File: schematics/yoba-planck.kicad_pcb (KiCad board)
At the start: 2 copper layers, 60 parts, among them M1 AUDIO-JACK3, M2 AUDIO-JACK3, M3 ARDUINO_PRO_MICRO, SW1 SW_PUSH, SW10 SW_PUSH, SW11 SW_PUSH, SW12 SW_PUSH, SW13 SW_PUSH, SW14 SW_PUSH, SW15 SW_PUSH, SW16 SW_PUSH, SW17 SW_PUSH, SW18 SW_PUSH, SW19 SW_PUSH, SW2 SW_PUSH, SW20 SW_PUSH, SW21 SW_PUSH, SW22 SW_PUSH, SW23 SW_PUSH, SW24 SW_PUSH, SW3 SW_PUSH, SW4 SW_PUSH, SW5 SW_PUSH, SW6 SW_PUSH, SW7 SW_PUSH, SW8 SW_PUSH, SW9 SW_PUSH

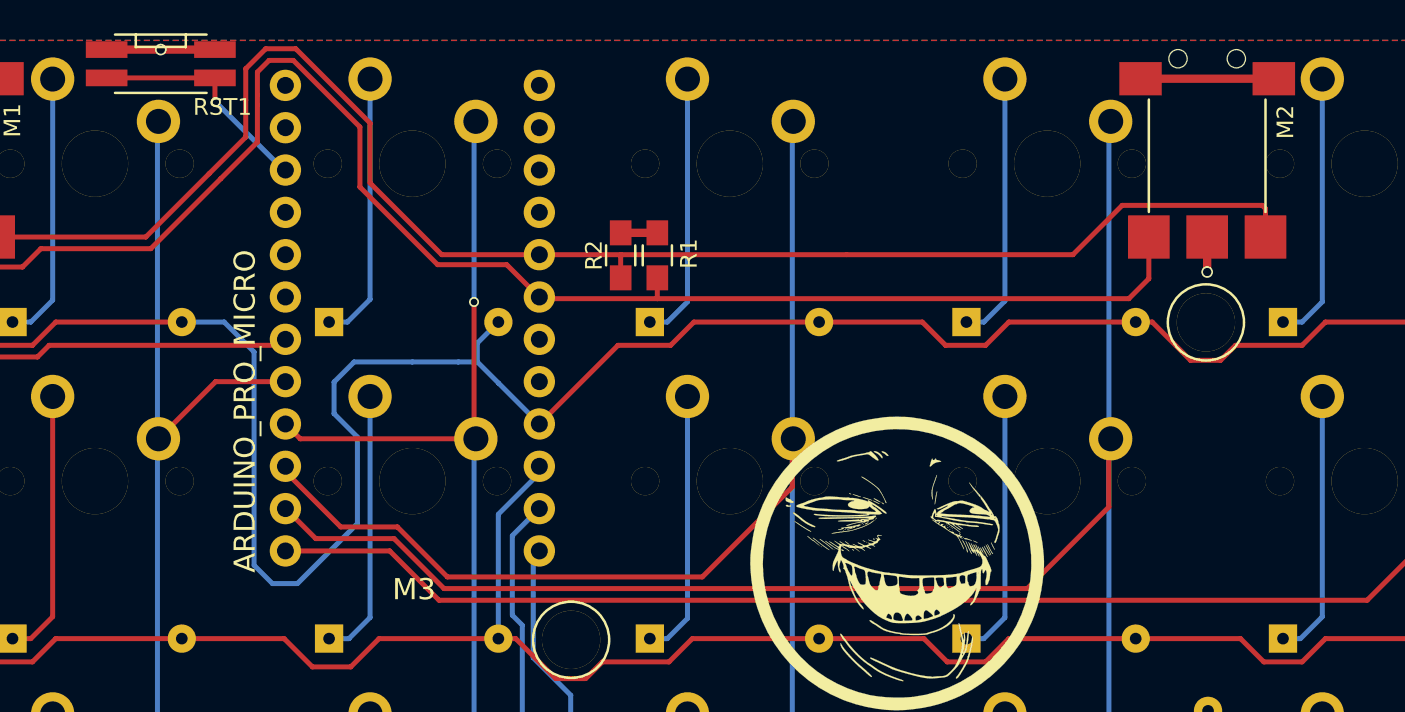
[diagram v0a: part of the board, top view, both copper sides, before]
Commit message: series resistance added to i2c bus
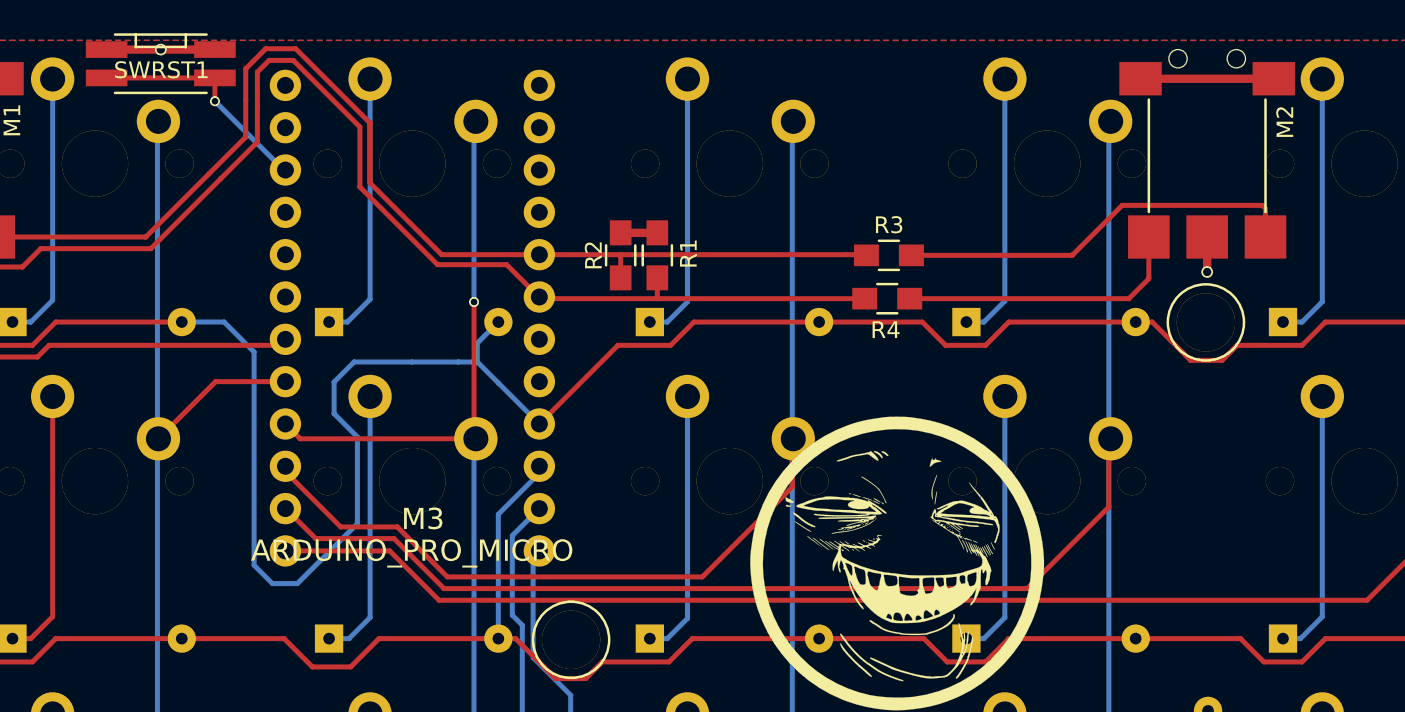
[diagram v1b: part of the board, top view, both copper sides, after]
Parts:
- removed RST1: SW_PUSH, yoba:edgeswbut
- added R3: 22, Resistors_SMD:R_0805_HandSoldering, F.Cu at (180.7, 75.5)
- added R4: 22, Resistors_SMD:R_0805_HandSoldering, F.Cu at (180.6, 78.1)
- added SWRST1: SW_PUSH, yoba:edgeswbut, F.Cu at (137.0, 64.0)
- M3: footprint SparkFun-Boards:ARDUINO_PRO_MICRO -> yoba:ARDUINO_PRO_MICRO
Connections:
- M2 pad 2: sda -> Net-(M2-Pad2)
- M2 pad 3: scl -> Net-(M2-Pad3)
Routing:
- net sda: track 95.1 -> 68.1 mm
- net Net-(M2-Pad2): track 0.00 -> 24.3 mm
- net scl: track 97.9 -> 77.6 mm
- net Net-(M2-Pad3): track 0.00 -> 17.5 mm

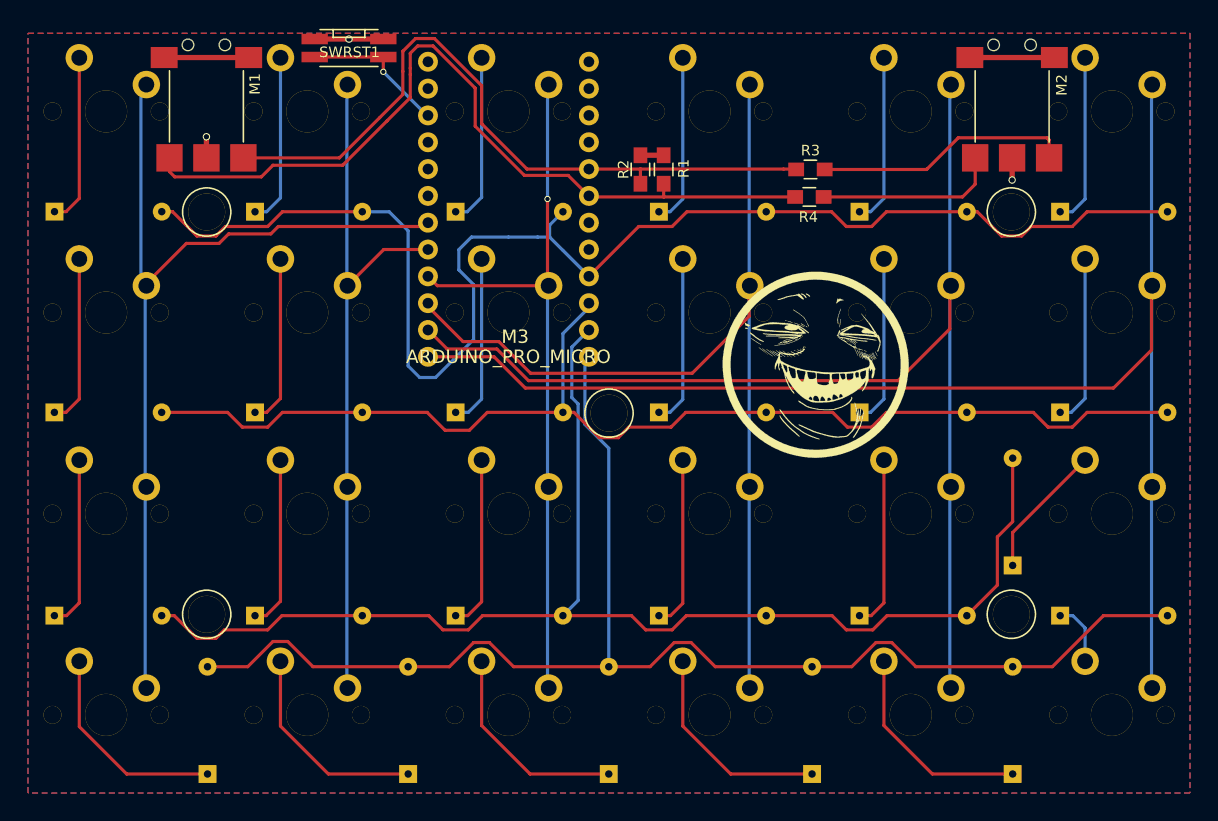
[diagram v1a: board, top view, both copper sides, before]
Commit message: Logo updated, layout improoved, mouting holes enlarged
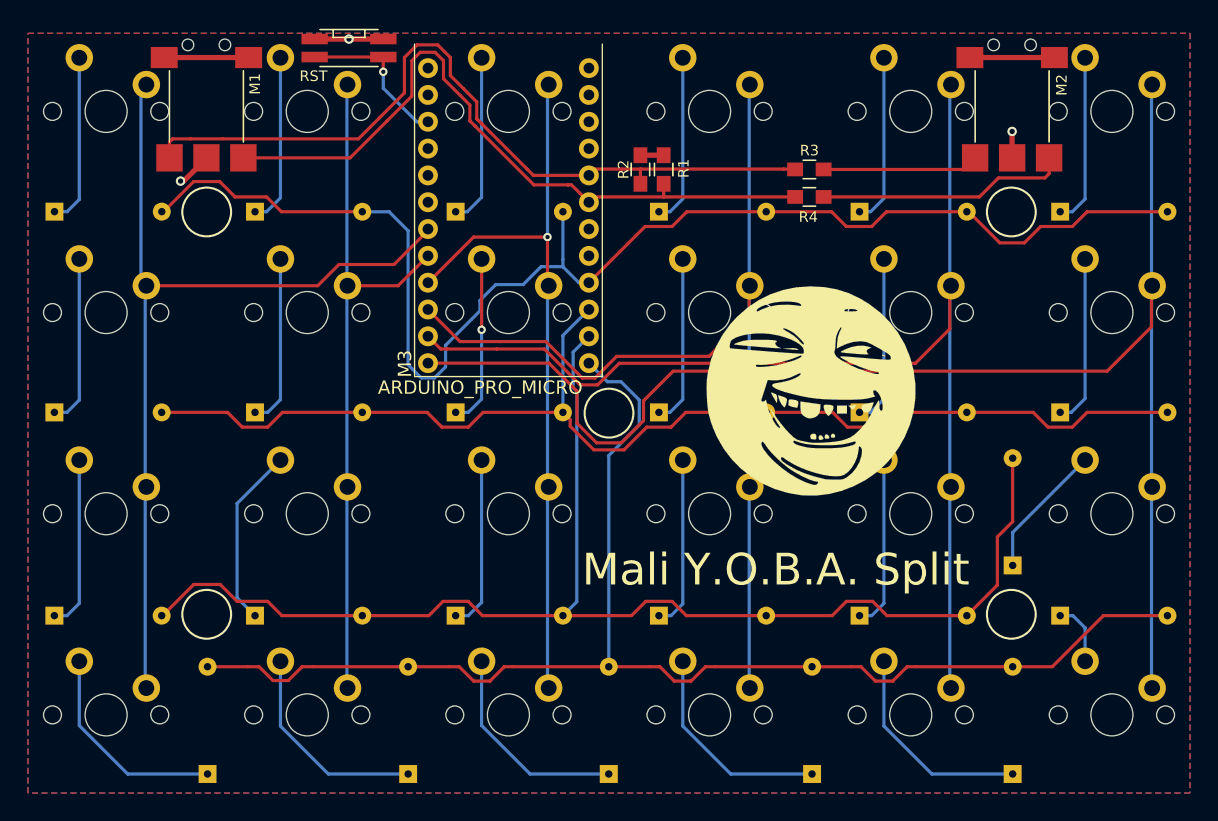
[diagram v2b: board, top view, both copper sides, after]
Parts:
- moved G*** 2.52 mm to (180.8, 96.5), turned to 0 degrees
- moved M3 0.60 mm to (152.1, 78.6)
- moved R3 0.10 mm to (180.6, 75.5)
- renumbered SWRST1 to RST
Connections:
- M1 pad 2: sda -> scl
- M1 pad 3: scl -> sda
- M3 pad 3: (no net) -> GND
- M3 pad 4: (no net) -> GND
- R3 pad 1: Net-(M2-Pad2) -> Net-(M2-Pad3)
- R4 pad 1: Net-(M2-Pad3) -> Net-(M2-Pad2)
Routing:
- net scl: track 77.6 -> 67.6 mm
- net sda: track 68.1 -> 75.3 mm
- net col5: track 134.7 -> 140.2 mm
- net row0: track 133.7 -> 130.5 mm
- net Net-(M2-Pad3): track 17.5 -> 14.9 mm
- net GND: track 10.6 -> 12.4 mm
- net col2: track 68.9 -> 70.2 mm
- net Net-(M3-Pad22): track 13.8 -> 15.0 mm
- net row3: track 131.0 -> 130.0 mm
- net Net-(D7-Pad1): track 16.3 -> 17.1 mm
- net Net-(M2-Pad2): track 24.3 -> 23.8 mm
- net Net-(D10-Pad1): vias 0 -> 1
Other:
- net class Default: via_dia 0.6 -> 0.8
- net class power: via_dia 0.7 -> 0.9
- board text added: "Mali Y.O.B.A. Split"

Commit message: fixed board outline
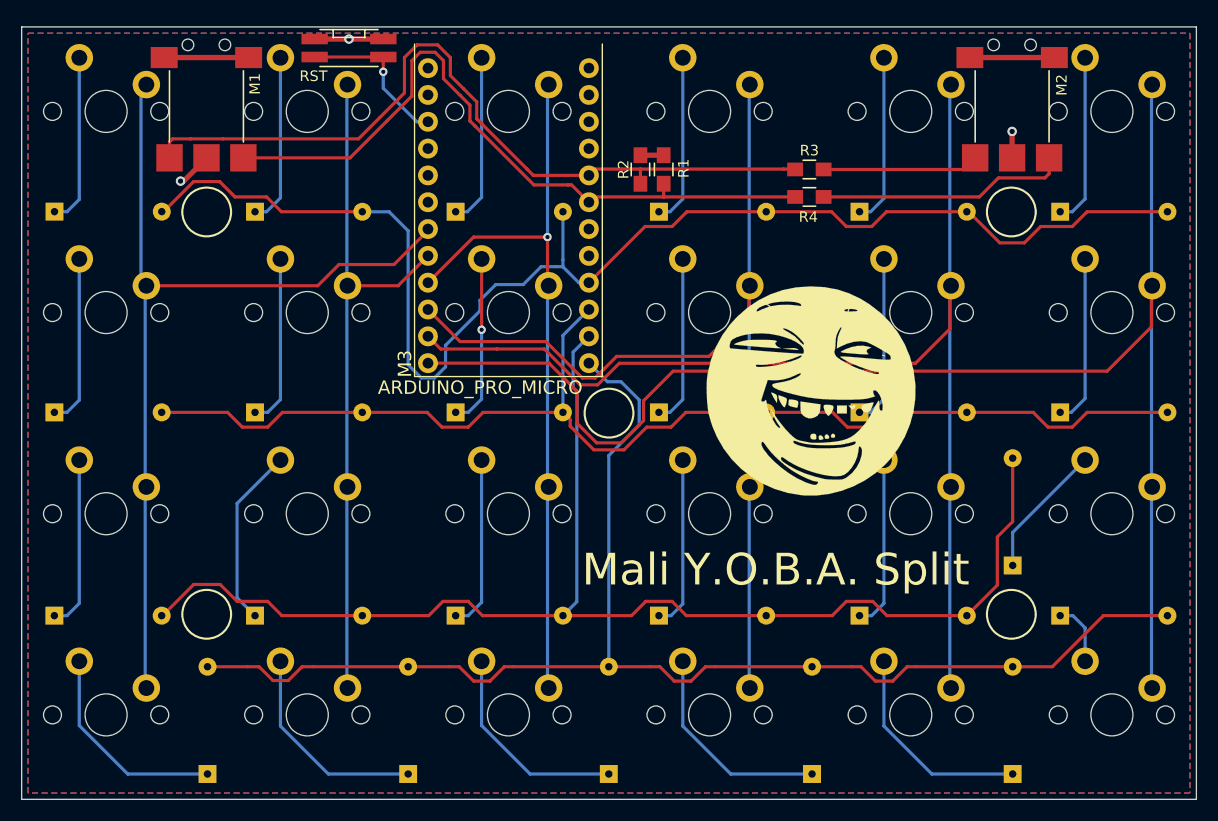
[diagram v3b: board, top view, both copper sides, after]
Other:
- board outline added: 111.2 x 73.2 mm
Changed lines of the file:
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@@
     (links 94)
     (no_connects 0)
-    (area 105.889499 56.15 229.35 138.0291)
+    (area 105.889499 56.45 227.15 138.0291)
     (thickness 1.6)
-    (drawings 9)
+    (drawings 7)
     (tracks 387)
     (zones 0)
@@
       (xy -4.275171 -4.863703)) (layer F.SilkS) (width 0.01))
   )
-  (gr_line (start 217 62) (end 217.25 62) (angle 90) (layer F.Fab) (width 0.2))
-  (gr_line (start 217.25 135.15) (end 217.25 135) (angle 90) (layer F.Fab) (width 0.2))
-  (gr_line (start 217 135.15) (end 217.25 135.15) (angle 90) (layer F.Fab) (width 0.2))
-  (gr_line (start 106 135) (end 106 135.15) (angle 90) (layer F.Fab) (width 0.2))
+  (dimension 111.25 (width 0.3) (layer F.Fab)
+    (gr_text "111.250 mm" (at 161.625 57.8) (layer F.Fab)
+      (effects (font (size 1.5 1.5) (thickness 0.3)))
+    )
+    (feature1 (pts (xy 106 62) (xy 106 56.45)))
+    (feature2 (pts (xy 217.25 62) (xy 217.25 56.45)))
+    (crossbar (pts (xy 217.25 59.15) (xy 106 59.15)))
+    (arrow1a (pts (xy 106 59.15) (xy 107.126504 58.563579)))
+    (arrow1b (pts (xy 106 59.15) (xy 107.126504 59.736421)))
+    (arrow2a (pts (xy 217.25 59.15) (xy 216.123496 58.563579)))
+    (arrow2b (pts (xy 217.25 59.15) (xy 216.123496 59.736421)))
+  )
+  (dimension 73.15 (width 0.3) (layer F.Fab)
+    (gr_text "73.150 mm" (at 220.65 98.575 270) (layer F.Fab)
+      (effects (font (size 1.5 1.5) (thickness 0.3)))
+    )
+    (feature1 (pts (xy 217.25 135.15) (xy 222 135.15)))
+    (feature2 (pts (xy 217.25 62) (xy 222 62)))
+    (crossbar (pts (xy 219.3 62) (xy 219.3 135.15)))
+    (arrow1a (pts (xy 219.3 135.15) (xy 218.713579 134.023496)))
+    (arrow1b (pts (xy 219.3 135.15) (xy 219.886421 134.023496)))
+    (arrow2a (pts (xy 219.3 62) (xy 218.713579 63.126504)))
+    (arrow2b (pts (xy 219.3 62) (xy 219.886421 63.126504)))
+  )
+  (gr_line (start 217.25 62) (end 106 62) (angle 90) (layer Edge.Cuts) (width 0.1))
+  (gr_line (start 217.25 135.15) (end 106 135.15) (angle 90) (layer Edge.Cuts) (width 0.1))
+  (gr_line (start 217.25 62) (end 217.25 135.15) (angle 90) (layer Edge.Cuts) (width 0.1))
+  (gr_line (start 106 135.15) (end 106 62) (angle 90) (layer Edge.Cuts) (width 0.1))
   (gr_text "Mali Y.O.B.A. Split" (at 177.419 113.411) (layer F.SilkS)
     (effects (font (size 3 3) (thickness 0.4)))
   )
-  (gr_line (start 217.25 62) (end 217.25 135) (angle 90) (layer F.Fab) (width 0.2))
-  (gr_line (start 106 62) (end 217 62) (angle 90) (layer F.Fab) (width 0.2))
-  (gr_line (start 106 135) (end 106 62) (angle 90) (layer F.Fab) (width 0.2))
-  (gr_line (start 106 135.15) (end 217 135.15) (angle 90) (layer F.Fab) (width 0.2))
   (segment (start 123.5 74.4) (end 123.5 74.448048) (width 0.5) (layer F.Cu) (net 1))
   (segment (start 123.5 74.448048) (end 121.348048 76.6) (width 0.5) (layer F.Cu) (net 1))

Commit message: rev2
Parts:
- added C1: C, Capacitors_SMD:C_0805_HandSoldering, F.Cu at (179.7, 67.5)
- added D25: LED, mx1a:MX1A-led, F.Cu at (114.0, 70.0)
- added D26: LED, mx1a:MX1A-led, F.Cu at (114.0, 89.0)
- added D27: LED, mx1a:MX1A-led, F.Cu at (114.0, 108.1)
- added D28: LED, mx1a:MX1A-led, F.Cu at (114.0, 127.2)
- added D29: LED, mx1a:MX1A-led, F.Cu at (133.1, 70.0)
- added D30: LED, mx1a:MX1A-led, F.Cu at (133.1, 89.0)
- added D31: LED, mx1a:MX1A-led, F.Cu at (133.1, 108.1)
- added D32: LED, mx1a:MX1A-led, F.Cu at (133.1, 127.2)
- added D33: LED, mx1a:MX1A-led, F.Cu at (152.1, 70.0)
- added D34: LED, mx1a:MX1A-led, F.Cu at (152.1, 89.0)
- added D35: LED, mx1a:MX1A-led, F.Cu at (152.1, 108.1)
- added D36: LED, mx1a:MX1A-led, F.Cu at (152.1, 127.2)
- added D37: LED, mx1a:MX1A-led, F.Cu at (171.2, 70.0)
- added D38: LED, mx1a:MX1A-led, F.Cu at (171.2, 89.0)
- added D39: LED, mx1a:MX1A-led, F.Cu at (171.2, 108.1)
- added D40: LED, mx1a:MX1A-led, F.Cu at (171.2, 127.2)
- added D41: LED, mx1a:MX1A-led, F.Cu at (190.2, 70.0)
- added D42: LED, mx1a:MX1A-led, F.Cu at (190.2, 89.0)
- added D43: LED, mx1a:MX1A-led, F.Cu at (190.2, 108.1)
- added D44: LED, mx1a:MX1A-led, F.Cu at (190.2, 127.2)
- added D45: LED, mx1a:MX1A-led, F.Cu at (209.2, 70.0)
- added D46: LED, mx1a:MX1A-led, F.Cu at (209.2, 89.0)
- added D47: LED, mx1a:MX1A-led, F.Cu at (209.2, 108.1)
- added D48: LED, mx1a:MX1A-led, F.Cu at (209.2, 127.2)
- added Q1: BS170, TO_SOT_Packages_SMD:SOT-23_Handsoldering, F.Cu at (140.8, 83.4)
- added R10: 1k, Resistors_SMD:R_0805_HandSoldering, F.Cu at (131.7, 97.7)
- added R11: 1k, Resistors_SMD:R_0805_HandSoldering, F.Cu at (131.7, 116.7)
- added R12: 1k, Resistors_SMD:R_0805_HandSoldering, F.Cu at (129.7, 130.9)
- added R13: 1k, Resistors_SMD:R_0805_HandSoldering, F.Cu at (153.3, 79.0)
- added R14: 1k, Resistors_SMD:R_0805_HandSoldering, F.Cu at (150.7, 97.8)
- added R15: 1k, Resistors_SMD:R_0805_HandSoldering, F.Cu at (150.7, 116.7)
- added R16: 1k, Resistors_SMD:R_0805_HandSoldering, F.Cu at (148.7, 130.9)
- added R17: 1k, Resistors_SMD:R_0805_HandSoldering, F.Cu at (169.8, 78.6)
- added R18: 1k, Resistors_SMD:R_0805_HandSoldering, F.Cu at (169.8, 97.7)
- added R19: 1k, Resistors_SMD:R_0805_HandSoldering, F.Cu at (169.8, 116.7)
- added R20: 1k, Resistors_SMD:R_0805_HandSoldering, F.Cu at (167.7, 130.9)
- added R21: 1k, Resistors_SMD:R_0805_HandSoldering, F.Cu at (188.9, 78.6)
- added R22: 1k, Resistors_SMD:R_0805_HandSoldering, F.Cu at (188.9, 97.7)
- added R23: 1k, Resistors_SMD:R_0805_HandSoldering, F.Cu at (188.9, 116.7)
- added R24: 1k, Resistors_SMD:R_0805_HandSoldering, F.Cu at (186.8, 130.9)
- added R25: 1k, Resistors_SMD:R_0805_HandSoldering, F.Cu at (207.9, 78.6)
- added R26: 1k, Resistors_SMD:R_0805_HandSoldering, F.Cu at (207.9, 97.6)
- added R27: 1k, Resistors_SMD:R_0805_HandSoldering, F.Cu at (207.9, 116.8)
- added R28: 1k, Resistors_SMD:R_0805_HandSoldering, F.Cu at (205.8, 130.9)
- added R5: 1k, Resistors_SMD:R_0805_HandSoldering, F.Cu at (112.7, 78.7)
- added R6: 1k, Resistors_SMD:R_0805_HandSoldering, F.Cu at (112.7, 97.7)
- added R7: 1k, Resistors_SMD:R_0805_HandSoldering, F.Cu at (112.7, 116.7)
- added R8: 1k, Resistors_SMD:R_0805_HandSoldering, F.Cu at (110.6, 130.9)
- added R9: 1k, Resistors_SMD:R_0805_HandSoldering, F.Cu at (131.7, 78.7)
- M3: moved to F.Cu
- moved RST1 38.4 mm to (175.4, 64.0)
- moved R3 32.4 mm to (148.2, 74.4), turned to 270 degrees
- moved R4 29.8 mm to (150.8, 79.0), turned to 270 degrees
- moved D10 10.2 mm to (157.2, 98.5), turned to 180 degrees
- moved D11 10.2 mm to (157.2, 117.8), turned to 180 degrees
- moved D13 10.2 mm to (176.5, 79.5), turned to 180 degrees
- moved D14 10.2 mm to (176.5, 98.5), turned to 180 degrees
- moved D15 10.2 mm to (176.5, 117.8), turned to 180 degrees
- moved D17 10.2 mm to (195.5, 79.5), turned to 180 degrees
- moved D18 10.2 mm to (195.5, 98.5), turned to 180 degrees
- moved D19 10.2 mm to (195.5, 117.8), turned to 180 degrees
- moved D2 10.2 mm to (119.2, 98.5), turned to 180 degrees
- moved D21 10.2 mm to (214.5, 79.5), turned to 180 degrees
- moved D22 10.2 mm to (214.5, 98.5), turned to 180 degrees
- moved D3 10.2 mm to (119.2, 117.8), turned to 180 degrees
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- renumbered RST to RST1
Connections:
- D1 pad 1: Net-(D1-Pad1) -> row0
- D1 pad 2: row0 -> Net-(D1-Pad2)
- D10 pad 1: Net-(D10-Pad1) -> row1
- D10 pad 2: row1 -> Net-(D10-Pad2)
- D11 pad 1: Net-(D11-Pad1) -> row2
- D11 pad 2: row2 -> Net-(D11-Pad2)
- D12 pad 1: Net-(D12-Pad1) -> row3
- D12 pad 2: row3 -> Net-(D12-Pad2)
- D13 pad 1: Net-(D13-Pad1) -> row0
- D13 pad 2: row0 -> Net-(D13-Pad2)
- D14 pad 1: Net-(D14-Pad1) -> row1
- D14 pad 2: row1 -> Net-(D14-Pad2)
- D15 pad 1: Net-(D15-Pad1) -> row2
- D15 pad 2: row2 -> Net-(D15-Pad2)
- D16 pad 1: Net-(D16-Pad1) -> row3
- D16 pad 2: row3 -> Net-(D16-Pad2)
- D17 pad 1: Net-(D17-Pad1) -> row0
- D17 pad 2: row0 -> Net-(D17-Pad2)
- D18 pad 1: Net-(D18-Pad1) -> row1
- D18 pad 2: row1 -> Net-(D18-Pad2)
- D19 pad 1: Net-(D19-Pad1) -> row2
- D19 pad 2: row2 -> Net-(D19-Pad2)
- D2 pad 1: Net-(D2-Pad1) -> row1
- D2 pad 2: row1 -> Net-(D2-Pad2)
- D20 pad 1: Net-(D20-Pad1) -> row3
- D20 pad 2: row3 -> Net-(D20-Pad2)
- D21 pad 1: Net-(D21-Pad1) -> row0
- D21 pad 2: row0 -> Net-(D21-Pad2)
- D22 pad 1: Net-(D22-Pad1) -> row1
- D22 pad 2: row1 -> Net-(D22-Pad2)
- D23 pad 1: Net-(D23-Pad1) -> row2
- D23 pad 2: row2 -> Net-(D23-Pad2)
- D24 pad 1: Net-(D24-Pad1) -> row3
- D24 pad 2: row3 -> Net-(D24-Pad2)
- D3 pad 1: Net-(D3-Pad1) -> row2
- D3 pad 2: row2 -> Net-(D3-Pad2)
- D4 pad 1: Net-(D4-Pad1) -> row3
- D4 pad 2: row3 -> Net-(D4-Pad2)
- D5 pad 1: Net-(D5-Pad1) -> row0
- D5 pad 2: row0 -> Net-(D5-Pad2)
- D6 pad 1: Net-(D6-Pad1) -> row1
- D6 pad 2: row1 -> Net-(D6-Pad2)
- D7 pad 1: Net-(D7-Pad1) -> row2
- D7 pad 2: row2 -> Net-(D7-Pad2)
- D8 pad 1: Net-(D8-Pad1) -> row3
- D8 pad 2: row3 -> Net-(D8-Pad2)
- D9 pad 1: Net-(D9-Pad1) -> row0
- D9 pad 2: row0 -> Net-(D9-Pad2)
- M1 pad 2: scl -> Net-(M1-Pad2)
- M1 pad 3: sda -> Net-(M1-Pad3)
- M2 pad 2: Net-(M2-Pad2) -> Net-(M1-Pad2)
- M2 pad 3: Net-(M2-Pad3) -> Net-(M1-Pad3)
- M3 pad 8: (no net) -> backlight
- R1 pad 2: scl -> Net-(M1-Pad2)
- R2 pad 2: sda -> Net-(M1-Pad3)
- R3 pad 1: Net-(M2-Pad3) -> Net-(M1-Pad3)
- R4 pad 1: Net-(M2-Pad2) -> Net-(M1-Pad2)
- SW1 pad 2: Net-(D1-Pad1) -> Net-(D1-Pad2)
- SW10 pad 2: Net-(D10-Pad1) -> Net-(D10-Pad2)
- SW11 pad 2: Net-(D11-Pad1) -> Net-(D11-Pad2)
- SW12 pad 2: Net-(D12-Pad1) -> Net-(D12-Pad2)
- SW13 pad 2: Net-(D13-Pad1) -> Net-(D13-Pad2)
- SW14 pad 2: Net-(D14-Pad1) -> Net-(D14-Pad2)
- SW15 pad 2: Net-(D15-Pad1) -> Net-(D15-Pad2)
- SW16 pad 2: Net-(D16-Pad1) -> Net-(D16-Pad2)
- SW17 pad 2: Net-(D17-Pad1) -> Net-(D17-Pad2)
- SW18 pad 2: Net-(D18-Pad1) -> Net-(D18-Pad2)
- SW19 pad 2: Net-(D19-Pad1) -> Net-(D19-Pad2)
- SW2 pad 2: Net-(D2-Pad1) -> Net-(D2-Pad2)
- SW20 pad 2: Net-(D20-Pad1) -> Net-(D20-Pad2)
- SW21 pad 2: Net-(D21-Pad1) -> Net-(D21-Pad2)
- SW22 pad 2: Net-(D22-Pad1) -> Net-(D22-Pad2)
- SW23 pad 2: Net-(D23-Pad1) -> Net-(D23-Pad2)
- SW24 pad 2: Net-(D24-Pad1) -> Net-(D24-Pad2)
- SW3 pad 2: Net-(D3-Pad1) -> Net-(D3-Pad2)
- SW4 pad 2: Net-(D4-Pad1) -> Net-(D4-Pad2)
- SW5 pad 2: Net-(D5-Pad1) -> Net-(D5-Pad2)
- SW6 pad 2: Net-(D6-Pad1) -> Net-(D6-Pad2)
- SW7 pad 2: Net-(D7-Pad1) -> Net-(D7-Pad2)
- SW8 pad 2: Net-(D8-Pad1) -> Net-(D8-Pad2)
- SW9 pad 2: Net-(D9-Pad1) -> Net-(D9-Pad2)
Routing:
- net Net-(Q1-Pad1): track 0.00 -> 468.4 mm
- net Net-(M1-Pad2): track 0.00 -> 92.2 mm
- net Net-(M1-Pad3): track 0.00 -> 91.0 mm
- net sda: track 75.3 -> 7.37 mm
- net scl: track 67.6 -> 9.40 mm
- net col5: track 140.2 -> 116.2 mm
- net Net-(M2-Pad2): track 23.8 -> 0.00 mm
- net col0: track 86.8 -> 107.9 mm, vias 0 -> 1
- net Net-(D16-Pad1): track 20.3 -> 0.00 mm
- net Net-(D20-Pad1): track 20.2 -> 0.00 mm
- net Net-(D4-Pad1): track 20.1 -> 0.00 mm
- net Net-(D8-Pad1): track 20.1 -> 0.00 mm
- net Net-(D12-Pad1): track 20.0 -> 0.00 mm
- net col3: track 96.1 -> 76.7 mm
- net VCC: track 18.2 -> 0.00 mm
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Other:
- board text added: "+"
- board text added: "R1,R2 - 2k (only master) R3,R4 - 22 C1 - 1u"
- board text added: "R5-R28 3.3V (LEDs) 620 (R/G/Y/O)"
- board text added: "R5-R28 5V (LEDs) 680 (blue/white) 1.3k (R/G/Y/O)"
- board text added: "Rev 2"
